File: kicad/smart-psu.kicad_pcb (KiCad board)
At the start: 2 copper layers, 22 parts, among them J1 DC-IN, J2 LOAD, J3 frontpanel, Q1 MMBT3904, Q2 P2003EVG, SW1 SW_DIP_x02, U1 LM2596S-5, U2 AP1117-33, U3 ATtiny13-20SSU

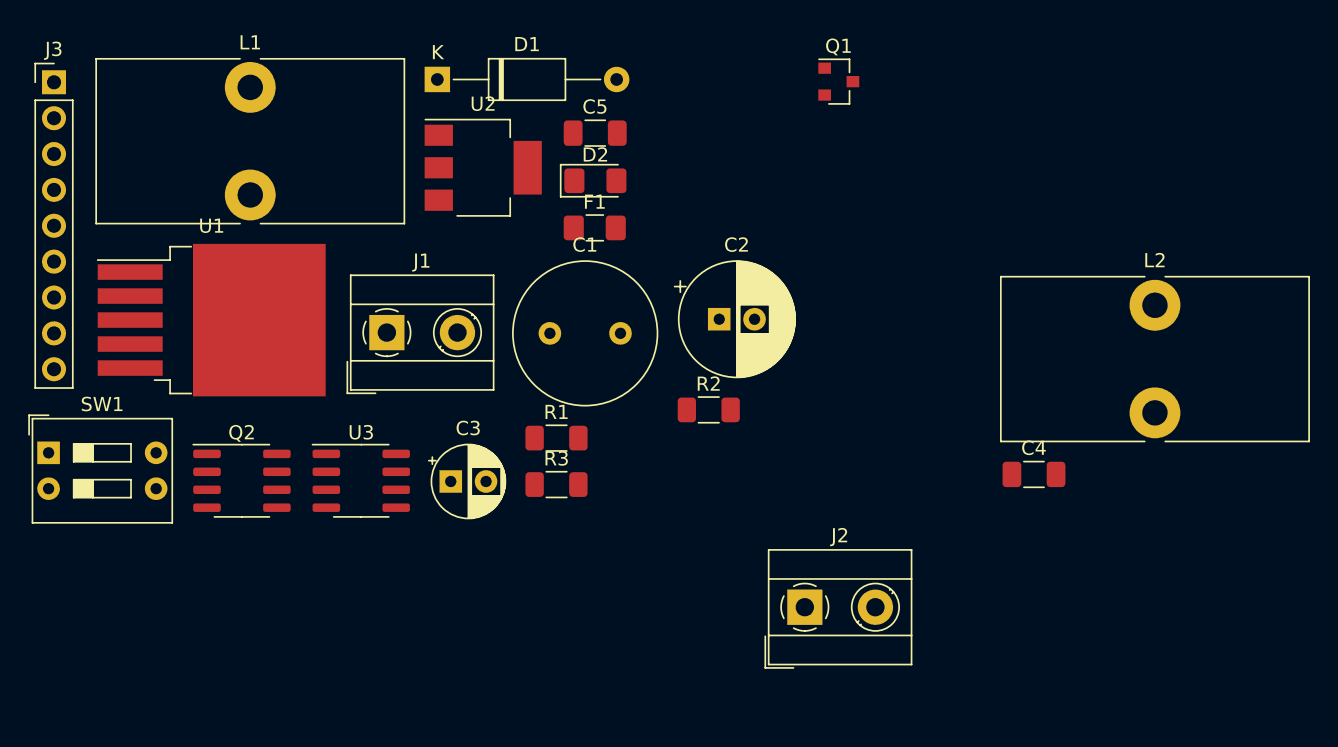
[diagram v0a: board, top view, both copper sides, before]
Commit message: Update frontpanel connector
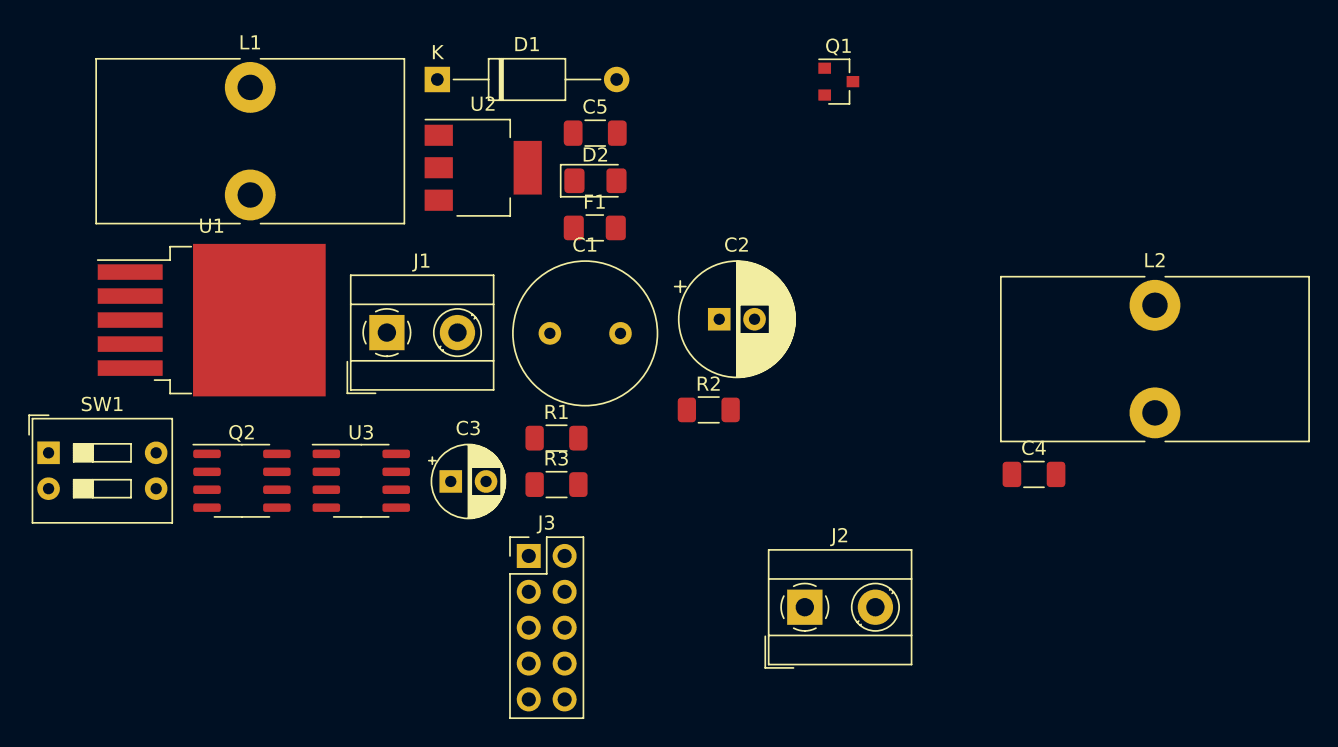
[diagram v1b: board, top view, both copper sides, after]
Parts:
- J3: footprint Connector_PinHeader_2.54mm:PinHeader_1x09_P2.54mm_Vertical -> Connector_PinHeader_2.54mm:PinHeader_2x05_P2.54mm_Vertical
- moved J3 47.5 mm to (44.5, 39.4)
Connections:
- J3 pad 2: /PWR_SW -> GND
- J3 pad 3: GND -> /PWR_SW
- J3 pad 4: /GPIO -> GND
- J3 pad 5: GND -> /GPIO
- J3 pad 6: /LOAD -> GND
- J3 pad 8: GND -> /LOAD
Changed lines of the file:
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@@
-(kicad_pcb (version 20171130) (host pcbnew "(5.1.9-0-10_14)")
+(kicad_pcb (version 20171130) (host pcbnew "(5.1.10-1-10_14)")
   (general
     (thickness 1.6)
@@
     (add_net "Net-(Q1-Pad1)")
     (add_net "Net-(Q1-Pad3)")
+  )
+  (module Connector_PinHeader_2.54mm:PinHeader_2x05_P2.54mm_Vertical (layer F.Cu)
+    (at 44.45 39.37)
+    (descr "Through hole straight pin header, 2x05, 2.54mm pitch, double rows")
+    (tags "Through hole pin header THT 2x05 2.54mm double row")
+    (fp_text reference J3 (at 1.27 -2.33) (layer F.SilkS)
+      (effects (font (size 1 1) (thickness 0.15)))
+    )
+    (fp_text value frontpanel (at 1.27 12.49) (layer F.Fab)
+      (effects (font (size 1 1) (thickness 0.15)))
+    )
+    (fp_line (start 4.35 -1.8) (end -1.8 -1.8) (layer F.CrtYd) (width 0.05))
+    (fp_line (start 4.35 11.95) (end 4.35 -1.8) (layer F.CrtYd) (width 0.05))
+    (fp_line (start -1.8 11.95) (end 4.35 11.95) (layer F.CrtYd) (width 0.05))
+    (fp_line (start -1.8 -1.8) (end -1.8 11.95) (layer F.CrtYd) (width 0.05))
+    (fp_line (start -1.33 -1.33) (end 0 -1.33) (layer F.SilkS) (width 0.12))
+    (fp_line (start -1.33 0) (end -1.33 -1.33) (layer F.SilkS) (width 0.12))
+    (fp_line (start 1.27 -1.33) (end 3.87 -1.33) (layer F.SilkS) (width 0.12))
+    (fp_line (start 1.27 1.27) (end 1.27 -1.33) (layer F.SilkS) (width 0.12))
+    (fp_line (start -1.33 1.27) (end 1.27 1.27) (layer F.SilkS) (width 0.12))
+    (fp_line (start 3.87 -1.33) (end 3.87 11.49) (layer F.SilkS) (width 0.12))
+    (fp_line (start -1.33 1.27) (end -1.33 11.49) (layer F.SilkS) (width 0.12))
+    (fp_line (start -1.33 11.49) (end 3.87 11.49) (layer F.SilkS) (width 0.12))
+    (fp_line (start -1.27 0) (end 0 -1.27) (layer F.Fab) (width 0.1))
+    (fp_line (start -1.27 11.43) (end -1.27 0) (layer F.Fab) (width 0.1))
+    (fp_line (start 3.81 11.43) (end -1.27 11.43) (layer F.Fab) (width 0.1))
+    (fp_line (start 3.81 -1.27) (end 3.81 11.43) (layer F.Fab) (width 0.1))
+    (fp_line (start 0 -1.27) (end 3.81 -1.27) (layer F.Fab) (width 0.1))
+    (fp_text user %R (at 1.27 5.08 90) (layer F.Fab)
+      (effects (font (size 1 1) (thickness 0.15)))
+    )
+    (pad 1 thru_hole rect (at 0 0) (size 1.7 1.7) (drill 1) (layers *.Cu *.Mask)
+      (net 18 "Net-(J3-Pad1)"))
+    (pad 2 thru_hole oval (at 2.54 0) (size 1.7 1.7) (drill 1) (layers *.Cu *.Mask)
+      (net 2 GND))
+    (pad 3 thru_hole oval (at 0 2.54) (size 1.7 1.7) (drill 1) (layers *.Cu *.Mask)
+      (net 14 /PWR_SW))
+    (pad 4 thru_hole oval (at 2.54 2.54) (size 1.7 1.7) (drill 1) (layers *.Cu *.Mask)
+      (net 2 GND))
+    (pad 5 thru_hole oval (at 0 5.08) (size 1.7 1.7) (drill 1) (layers *.Cu *.Mask)
+      (net 6 /GPIO))
+    (pad 6 thru_hole oval (at 2.54 5.08) (size 1.7 1.7) (drill 1) (layers *.Cu *.Mask)
+      (net 2 GND))
+    (pad 7 thru_hole oval (at 0 7.62) (size 1.7 1.7) (drill 1) (layers *.Cu *.Mask)
+      (net 7 /LOAD))
+    (pad 8 thru_hole oval (at 2.54 7.62) (size 1.7 1.7) (drill 1) (layers *.Cu *.Mask)
+      (net 7 /LOAD))
+    (pad 9 thru_hole oval (at 0 10.16) (size 1.7 1.7) (drill 1) (layers *.Cu *.Mask)
+      (net 2 GND))
+    (pad 10 thru_hole oval (at 2.54 10.16) (size 1.7 1.7) (drill 1) (layers *.Cu *.Mask)
+      (net 2 GND))
+    (model ${KISYS3DMOD}/Connector_PinHeader_2.54mm.3dshapes/PinHeader_2x05_P2.54mm_Vertical.wrl
+      (at (xyz 0 0 0))
+      (scale (xyz 1 1 1))
+      (rotate (xyz 0 0 0))
+    )
   )
   (module Capacitor_THT:C_Radial_D10.0mm_H20.0mm_P5.00mm (layer F.Cu)
@@
     )
   )
-  (module Connector_PinHeader_2.54mm:PinHeader_1x09_P2.54mm_Vertical (layer F.Cu)
-    (at 10.825001 5.825001)
-    (descr "Through hole straight pin header, 1x09, 2.54mm pitch, single row")
-    (tags "Through hole pin header THT 1x09 2.54mm single row")
-    (fp_text reference J3 (at 0 -2.33) (layer F.SilkS)
-      (effects (font (size 1 1) (thickness 0.15)))
-    )
-    (fp_text value frontpanel (at 0 22.65) (layer F.Fab)
-      (effects (font (size 1 1) (thickness 0.15)))
-    )
-    (fp_line (start 1.8 -1.8) (end -1.8 -1.8) (layer F.CrtYd) (width 0.05))
-    (fp_line (start 1.8 22.1) (end 1.8 -1.8) (layer F.CrtYd) (width 0.05))
-    (fp_line (start -1.8 22.1) (end 1.8 22.1) (layer F.CrtYd) (width 0.05))
-    (fp_line (start -1.8 -1.8) (end -1.8 22.1) (layer F.CrtYd) (width 0.05))
-    (fp_line (start -1.33 -1.33) (end 0 -1.33) (layer F.SilkS) (width 0.12))
-    (fp_line (start -1.33 0) (end -1.33 -1.33) (layer F.SilkS) (width 0.12))
-    (fp_line (start -1.33 1.27) (end 1.33 1.27) (layer F.SilkS) (width 0.12))
-    (fp_line (start 1.33 1.27) (end 1.33 21.65) (layer F.SilkS) (width 0.12))
-    (fp_line (start -1.33 1.27) (end -1.33 21.65) (layer F.SilkS) (width 0.12))
-    (fp_line (start -1.33 21.65) (end 1.33 21.65) (layer F.SilkS) (width 0.12))
-    (fp_line (start -1.27 -0.635) (end -0.635 -1.27) (layer F.Fab) (width 0.1))
-    (fp_line (start -1.27 21.59) (end -1.27 -0.635) (layer F.Fab) (width 0.1))
-    (fp_line (start 1.27 21.59) (end -1.27 21.59) (layer F.Fab) (width 0.1))
-    (fp_line (start 1.27 -1.27) (end 1.27 21.59) (layer F.Fab) (width 0.1))
-    (fp_line (start -0.635 -1.27) (end 1.27 -1.27) (layer F.Fab) (width 0.1))
-    (fp_text user %R (at 0 10.16 90) (layer F.Fab)
-      (effects (font (size 1 1) (thickness 0.15)))
-    )
-    (pad 1 thru_hole rect (at 0 0) (size 1.7 1.7) (drill 1) (layers *.Cu *.Mask)
-      (net 18 "Net-(J3-Pad1)"))
-    (pad 2 thru_hole oval (at 0 2.54) (size 1.7 1.7) (drill 1) (layers *.Cu *.Mask)
-      (net 14 /PWR_SW))
-    (pad 3 thru_hole oval (at 0 5.08) (size 1.7 1.7) (drill 1) (layers *.Cu *.Mask)
-      (net 2 GND))
-    (pad 4 thru_hole oval (at 0 7.62) (size 1.7 1.7) (drill 1) (layers *.Cu *.Mask)
-      (net 6 /GPIO))
-    (pad 5 thru_hole oval (at 0 10.16) (size 1.7 1.7) (drill 1) (layers *.Cu *.Mask)
-      (net 2 GND))
-    (pad 6 thru_hole oval (at 0 12.7) (size 1.7 1.7) (drill 1) (layers *.Cu *.Mask)
-      (net 7 /LOAD))
-    (pad 7 thru_hole oval (at 0 15.24) (size 1.7 1.7) (drill 1) (layers *.Cu *.Mask)
-      (net 7 /LOAD))
-    (pad 8 thru_hole oval (at 0 17.78) (size 1.7 1.7) (drill 1) (layers *.Cu *.Mask)
-      (net 2 GND))
-    (pad 9 thru_hole oval (at 0 20.32) (size 1.7 1.7) (drill 1) (layers *.Cu *.Mask)
-      (net 2 GND))
-    (model ${KISYS3DMOD}/Connector_PinHeader_2.54mm.3dshapes/PinHeader_1x09_P2.54mm_Vertical.wrl
-      (at (xyz 0 0 0))
-      (scale (xyz 1 1 1))
-      (rotate (xyz 0 0 0))
-    )
-  )
   (module Inductor_THT:L_Toroid_Vertical_L21.6mm_W11.4mm_P7.62mm_Pulse_KM-3 (layer F.Cu)
     (at 24.725001 6.185001)
@@
       (effects (font (size 1 1) (thickness 0.15)))
     )
-    (fp_text user %R (at 2.5 3) (layer F.Fab)
-      (effects (font (size 1 1) (thickness 0.15)))
-    )
-    (fp_arc (start 0 0) (end -0.789 1.484) (angle -29) (layer F.SilkS) (width 0.12))
-    (fp_arc (start 0 0) (end -1.484 -0.789) (angle -56) (layer F.SilkS) (width 0.12))
-    (fp_arc (start 0 0) (end 0.789 -1.484) (angle -56) (layer F.SilkS) (width 0.12))
-    (fp_arc (start 0 0) (end 1.484 0.789) (angle -56) (layer F.SilkS) (width 0.12))
-    (fp_arc (start 0 0) (end 0 1.68) (angle -28) (layer F.SilkS) (width 0.12))
     (fp_circle (center 0 0) (end 1.5 0) (layer F.Fab) (width 0.1))
     (fp_circle (center 5 0) (end 6.5 0) (layer F.Fab) (width 0.1))
@@
     (fp_line (start 8 4.5) (end 8 -4.5) (layer F.CrtYd) (width 0.05))
     (fp_line (start 8 -4.5) (end -3 -4.5) (layer F.CrtYd) (width 0.05))
+    (fp_text user %R (at 2.5 3) (layer F.Fab)
+      (effects (font (size 1 1) (thickness 0.15)))
+    )
+    (fp_arc (start 0 0) (end -0.789 1.484) (angle -29) (layer F.SilkS) (width 0.12))
+    (fp_arc (start 0 0) (end -1.484 -0.789) (angle -56) (layer F.SilkS) (width 0.12))
+    (fp_arc (start 0 0) (end 0.789 -1.484) (angle -56) (layer F.SilkS) (width 0.12))
+    (fp_arc (start 0 0) (end 1.484 0.789) (angle -56) (layer F.SilkS) (width 0.12))
+    (fp_arc (start 0 0) (end 0 1.68) (angle -28) (layer F.SilkS) (width 0.12))
     (pad 2 thru_hole circle (at 5 0) (size 2.5 2.5) (drill 1.3) (layers *.Cu *.Mask)
       (net 2 GND))
